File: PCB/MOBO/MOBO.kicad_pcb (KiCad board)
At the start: 2 copper layers, 77.5 x 78.7 mm, 93 parts, among them J101 COMP_OUT, J102 COMP_5V, J103 COMP_GND, J104 RPi_GPio, J105 JST_02, J106 RPi_SDA0, J107 RPi_TV, J108 RPi_D-, J109 RPi_D+, J110 RPi_SCL0, J111 RPi_Ts5V, J112 RPi_TsGND, J201 MAIN-USBC-OTG/PWR, Q201 AO3401A, Q202 FS8205A, Q203 IRLML6344, Q204 Si4435DDY, SW201 PCM12SMTR, SW301 RS Button, SW302 LS Button, SW303 DPAD Right, SW304 DPAD Left, SW306 B Button, SW307 A Button, SW308 DPAD Down, SW309 DPAD Up, U201 DW01A, U202 LC709203FQH-01TWG, U203 MCP73871-1AA, U204 TPS61230DRC, U301 ATmega328PB-M, Y301 YABM11-16.000MHZ-12-B1U-T

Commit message: Placed footprints
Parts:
- D201, D202, R214, R215: moved to B.Cu
- H105: moved to F.Cu
- moved R215 163.5 mm to (94.1, 51.1)
- moved R214 162.3 mm to (94.1, 55.1)
- moved C204 151.5 mm to (115.9, 50.4), turned to 180 degrees
- moved R211 146.0 mm to (107.0, 59.0), turned to 180 degrees
- moved C203 145.7 mm to (119.4, 60.8)
- moved R216 140.7 mm to (121.5, 38.5), turned to 90 degrees
- moved R206 137.9 mm to (115.3, 45.7), turned to 180 degrees
- moved R204 135.6 mm to (115.3, 47.7), turned to 180 degrees
- moved R202 131.4 mm to (115.6, 61.9), turned to 180 degrees
- moved R217 130.3 mm to (125.5, 70.7), turned to 180 degrees
- moved R213 130.1 mm to (126.1, 56.4), turned to 180 degrees
- moved R212 128.2 mm to (126.1, 58.4)
- moved R208 127.0 mm to (127.3, 46.4)
- moved R205 125.9 mm to (127.3, 44.4)
- moved R207 125.9 mm to (127.3, 48.4), turned to 180 degrees
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- renumbered J102 to 5V, J111 to 5V, J107 to Composite, J101 to Composite, J109 to D+, J108 to D-, J103 to GND, J112 to GND, J110 to SCL, J106 to SDA, SCK to SK

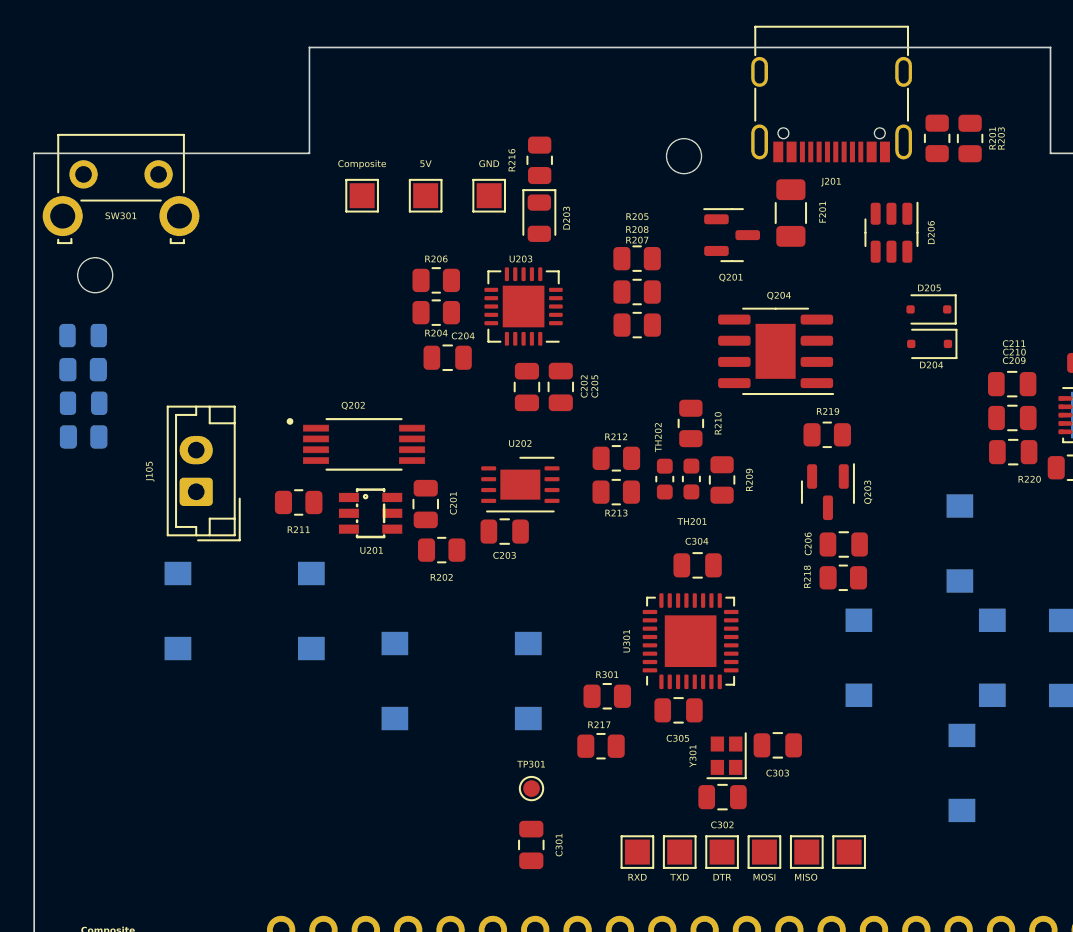
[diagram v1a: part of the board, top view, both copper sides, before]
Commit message: Started pcb traces
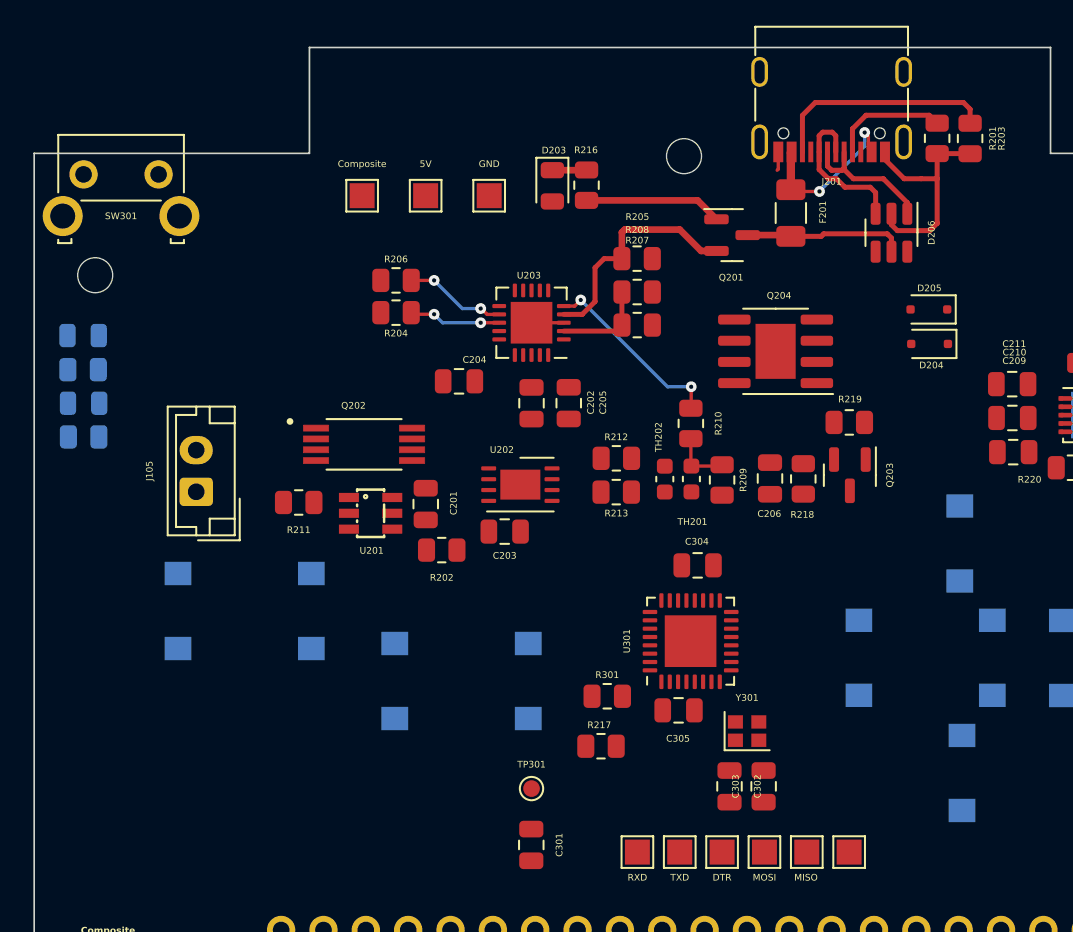
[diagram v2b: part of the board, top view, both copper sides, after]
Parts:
- moved R218 6.40 mm to (137.3, 57.6), turned to -90 degrees
- moved C206 5.94 mm to (135.3, 57.6), turned to -90 degrees
- moved R216 3.18 mm to (124.3, 40.0), turned to -90 degrees
- moved C303 2.60 mm to (134.9, 76.1), turned to 90 degrees
- moved R204 2.41 mm to (112.8, 47.7)
- moved R206 2.41 mm to (112.8, 45.7)
- moved D203 2.09 mm to (122.2, 40.0)
- moved Y301 1.93 mm to (133.9, 72.8), turned to 0 degrees
- moved Q203 1.66 mm to (140.1, 57.4)
- moved C204 1.57 mm to (116.6, 51.8)
- moved R219 1.52 mm to (140.0, 54.2)
- moved C205 1.08 mm to (123.2, 53.1)
- moved U203 1.08 mm to (121.0, 48.3)
- moved C202 1.01 mm to (121.0, 53.1)
- moved C302 0.77 mm to (132.9, 76.1), turned to -90 degrees
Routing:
- net GND: track 0.00 -> 25.3 mm
- net +5VD: track 0.00 -> 13.9 mm
- net CC2: track 0.00 -> 13.6 mm
- net THERM: track 0.00 -> 11.2 mm, vias 0 -> 2
- net VBUS: track 0.00 -> 10.0 mm, vias 0 -> 2
- net +5VA: track 0.00 -> 9.64 mm
- net /Power & Charging/D-_IN: track 0.00 -> 9.41 mm
- net /Power & Charging/D+_IN: track 0.00 -> 8.34 mm
- net CC1: track 0.00 -> 7.00 mm
- net PROG3: track 0.00 -> 6.12 mm, vias 0 -> 2
- net /Power & Charging/VPCC: track 0.00 -> 5.62 mm
- net PROG1: track 0.00 -> 5.53 mm, vias 0 -> 2
- net Net-(R209-Pad1): track 0.00 -> 3.53 mm
- net Net-(D203-K): track 0.00 -> 2.06 mm

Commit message: reviewed and staged some schematic changes to be done
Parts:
- moved R203 0.34 mm to (147.6, 37.4)
- moved R201 0.34 mm to (145.6, 37.4)
- moved D206 0.32 mm to (142.6, 43.2)
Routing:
- net VBUS: track 10.0 -> 22.0 mm
- net GND: track 25.3 -> 18.8 mm, vias 0 -> 5
- net THERM: track 11.2 -> 12.4 mm
- net /Power & Charging/D-_IN: track 9.41 -> 8.87 mm
